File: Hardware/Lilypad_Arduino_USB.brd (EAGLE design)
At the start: 50.8 x 50.8 mm, 45 parts, among them U1 MCP73831, U2 MIC5219, U3 ATMEGA32U41:1, Y1 8MHz

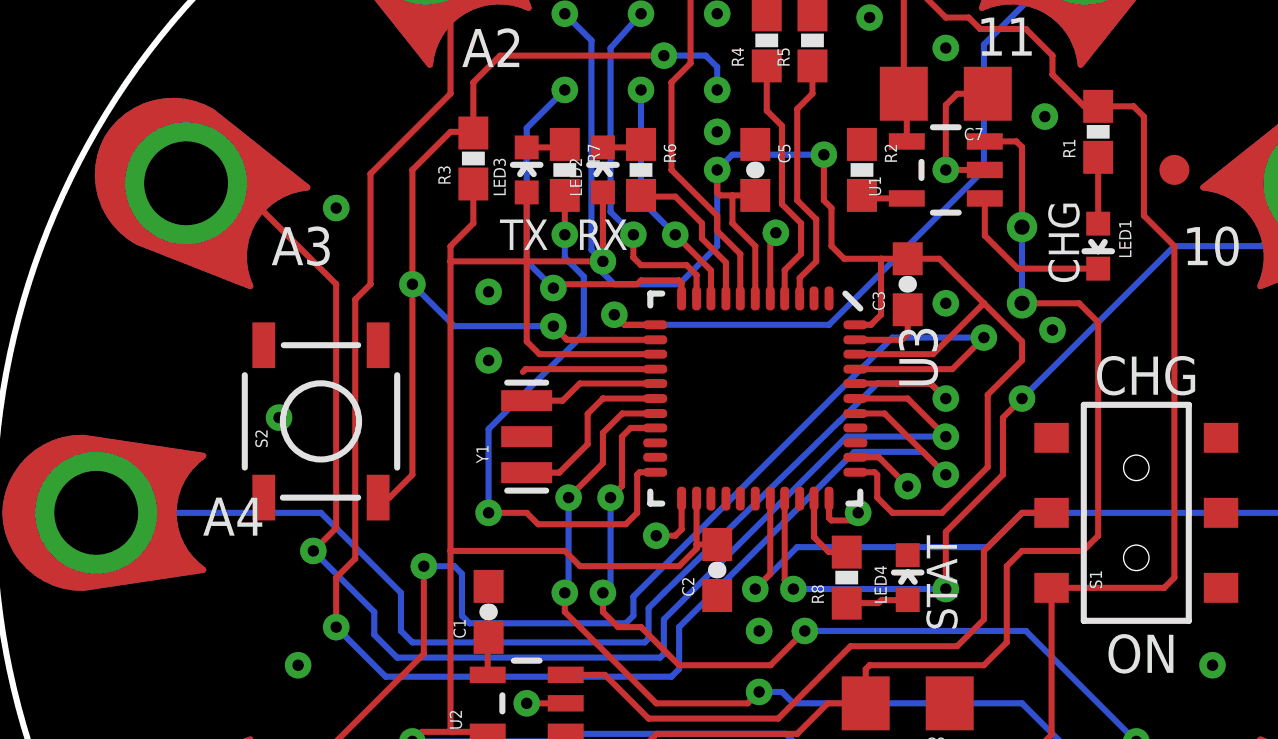
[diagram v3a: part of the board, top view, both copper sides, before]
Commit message: Minor silk changes
Moved A4 silk so it doesn't get cut off by the button pads. Added
Sparkfun flames in bottom silk.
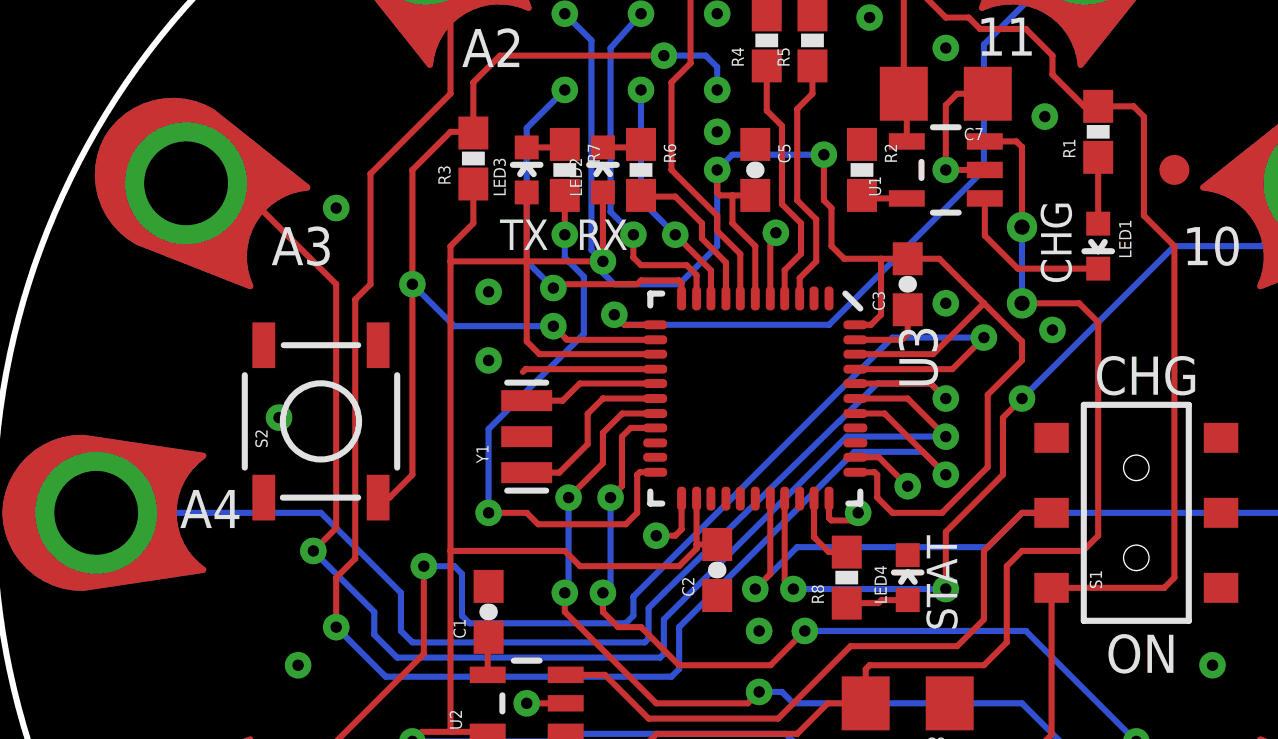
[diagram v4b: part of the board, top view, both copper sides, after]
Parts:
- added U$6: (no value), SparkFun-Aesthetics:SFE-LOGO-FLAME
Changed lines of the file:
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@@
 <text x="11.302996875" y="3.937" size="1.27" layer="21" font="vector" ratio="15">CHG</text>
 <text x="-16.001996875" y="-9.397996875" size="1.27" layer="21" font="vector" ratio="15">A5</text>
-<text x="-18.41499375" y="-0.762" size="1.27" layer="21" font="vector" ratio="15">A4</text>
+<text x="-19.17699375" y="-0.508" size="1.27" layer="21" font="vector" ratio="15">A4</text>
 <text x="-16.128996875" y="8.255" size="1.27" layer="21" font="vector" ratio="15">A3</text>
 <text x="-9.778996875" y="14.85899375" size="1.27" layer="21" font="vector" ratio="15">A2</text>
@@
 <rectangle x1="-2.54" y1="1.27" x2="2.54" y2="6.35" layer="41"/>
 <rectangle x1="2.667" y1="0.381" x2="2.921" y2="0.762" layer="41" rot="R180"/>
-<text x="10.795" y="7.62" size="1.016" layer="21" font="vector" ratio="15" rot="R90">CHG</text>
+<text x="10.541" y="7.62" size="1.016" layer="21" font="vector" ratio="15" rot="R90">CHG</text>
 <text x="6.731" y="-3.937" size="1.016" layer="21" font="vector" ratio="15" rot="R90">STAT</text>
 </plain>
@@
 <element name="U$1" library="LilyPad-Wearables" package="LOGO-LPA" value="LOGO-LPLPA" x="0" y="0" rot="MR0"/>
 <element name="U$5" library="SparkFun" package="OSHW-LOGO-M" value="OSHW-LOGOM" x="0" y="8.89" rot="MR0"/>
+<element name="U$6" library="SparkFun-Aesthetics" package="SFE-LOGO-FLAME" value="" x="0.762" y="2.794" rot="MR0"/>
 </elements>
 <signals>
